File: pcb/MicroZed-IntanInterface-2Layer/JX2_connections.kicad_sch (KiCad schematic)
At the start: 25 parts, among them Q2 BSS138, U3 FT230XS

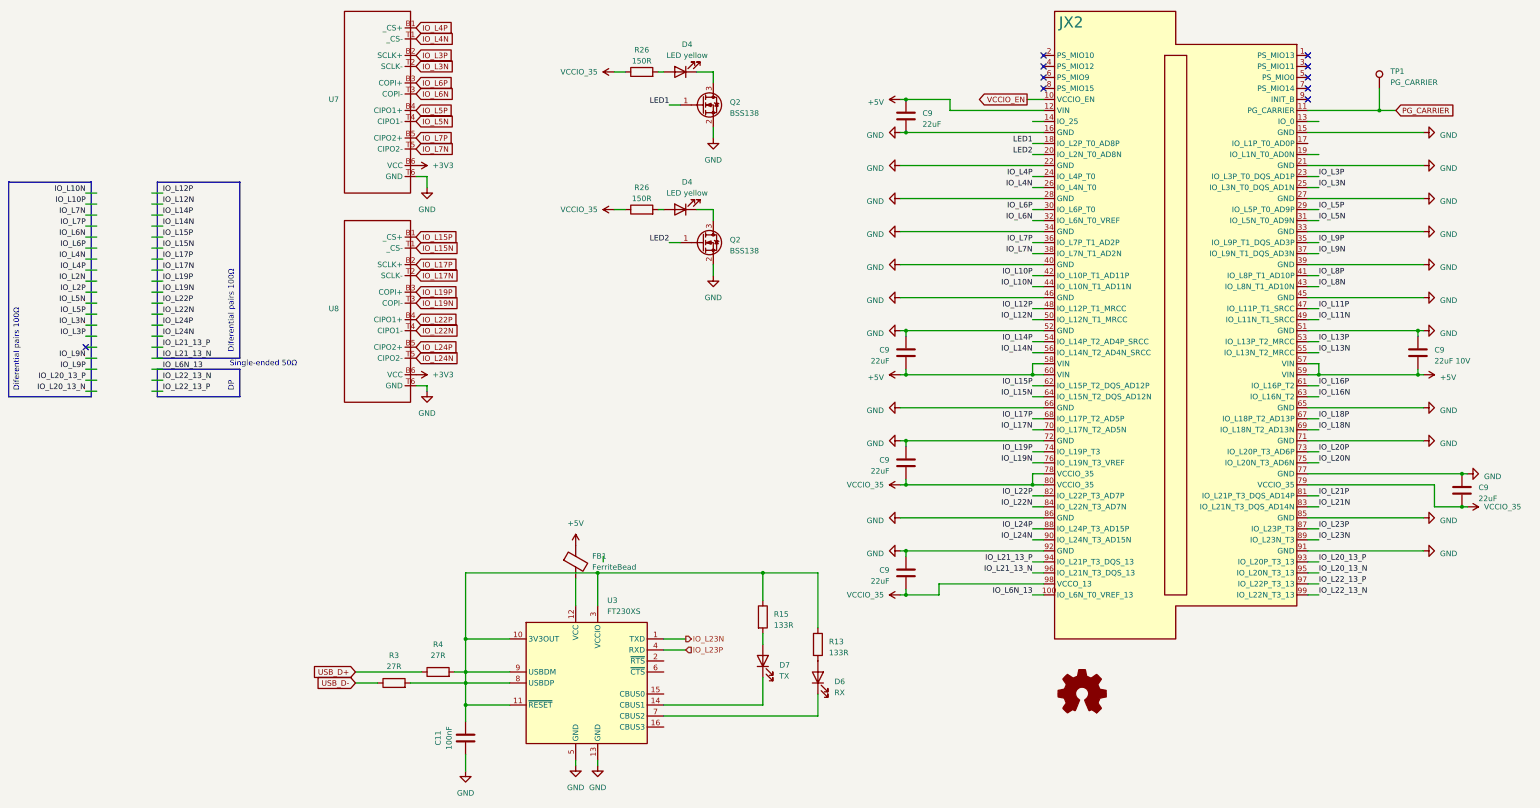
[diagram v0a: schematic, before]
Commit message: Updated PCB after v0.22 bug fixes
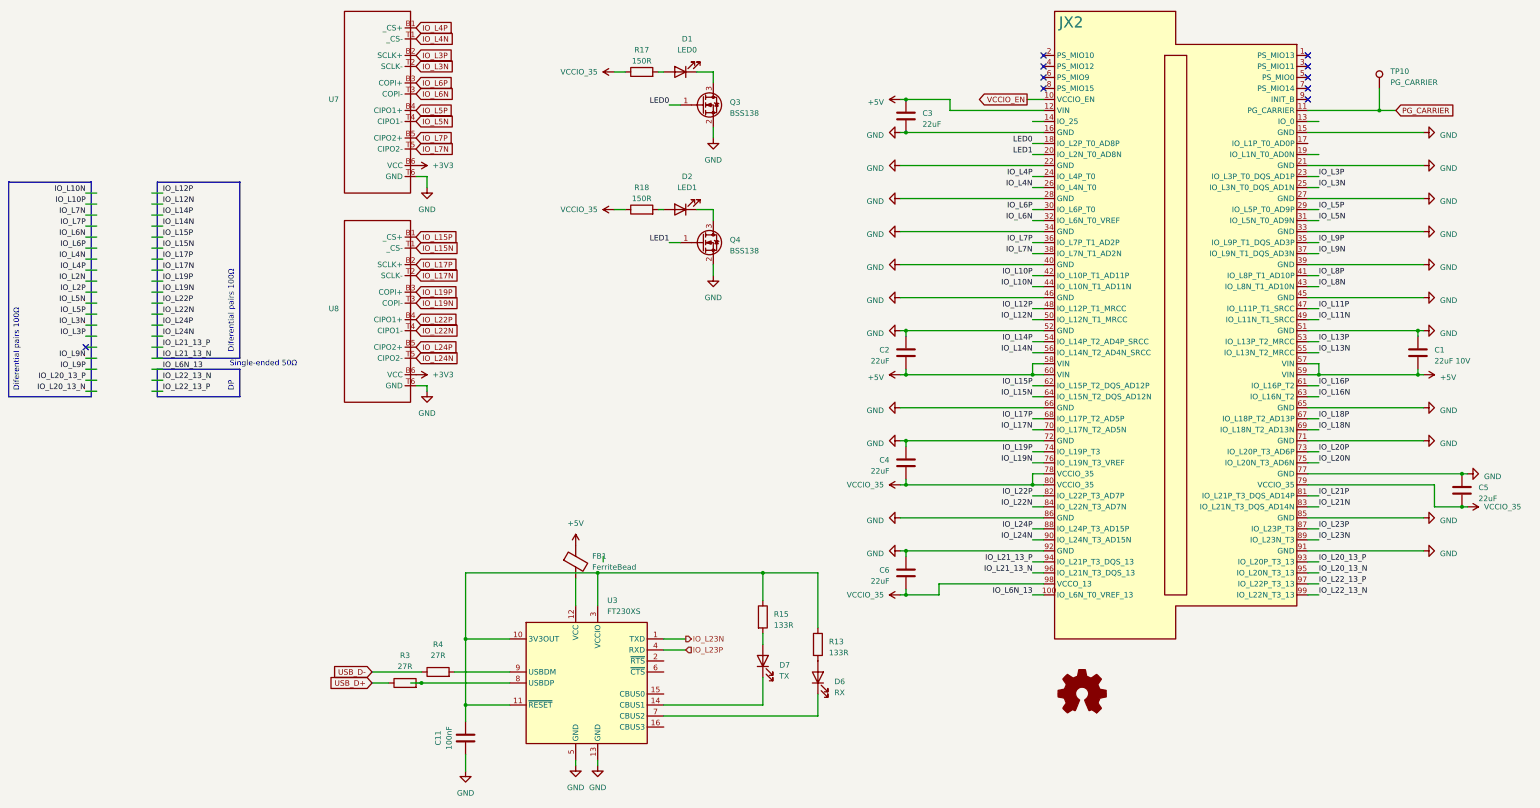
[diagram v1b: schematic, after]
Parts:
- removed D4 (x2): LED yellow, Viktor:LED0805, symbol Device:LED
- added D1: LED0, LED_SMD:LED_0603_1608Metric, symbol Device:LED
- added D2: LED1, LED_SMD:LED_0603_1608Metric, symbol Device:LED
- renumbered C9 to C1, C9 to C2, C9 to C3, C9 to C4, C9 to C5, C9 to C6, Q2 to Q3, Q2 to Q4, R26 to R17, R26 to R18, TP1 to TP10
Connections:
- net LED2 is gone; now on net LED1: JX2.20 (IO_L2N_T0_AD8N), Q4.1 (G)
- net LED1: no longer JX2.18 (IO_L2P_T0_AD8P), Q3.1 (G)
- net USB_D+: now also R3.1; no longer R4.1
- net USB_D-: now also R4.1; no longer R3.1
- net at C11.1, R13.1, R15.1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: no longer R3.2, R4.2, U3.8 (USBDP), U3.9 (USBDM)
- net at Q3.3 (D): now also D1.1 (K)
- net at Q4.3 (D): now also D2.1 (K)
- net at R17.2: now also D1.2 (A)
- net at R18.2: now also D2.2 (A)
- new net: R3.2, U3.8 (USBDP)
- new net: R4.2, U3.9 (USBDM)
- new net LED0: JX2.18 (IO_L2P_T0_AD8P), Q3.1 (G)
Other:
- moved on the sheet: R3

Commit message: Updates for version 1.0 to ship to UMich
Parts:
- C1: value 22uF 10V -> 22uF 25V; LCSC C5672 -> C12891
- C11: footprint Capacitor_SMD:C_0603_1608Metric -> Capacitor_SMD:C_0402_1005Metric; LCSC C66501 -> C307331
- C2, C3, C4, C5, C6: value 22uF -> 22uF 25V; LCSC C5672 -> C12891
- D1, D2, D6, D7: LCSC C2833058 -> C2286
- FB1: LCSC (none) -> C85840
- R13, R15: value 133R -> 150 1%; footprint Resistor_SMD:R_0603_1608Metric -> Resistor_SMD:R_0402_1005Metric; LCSC C4326496 -> C25082
- R17, R18: value 150R -> 150 1%; footprint Resistor_SMD:R_0603_1608Metric -> Resistor_SMD:R_0402_1005Metric; LCSC C22808 -> C25082
- R3, R4: value 27R -> 27; footprint Resistor_SMD:R_0603_1608Metric -> Resistor_SMD:R_0402_1005Metric; LCSC C4326496 -> C413051
- TP10: footprint Viktor:TestPoint__Drill1.0mm -> TestPoint:TestPoint_THTPad_D2.0mm_Drill1.0mm
- U3: LCSC (none) -> C69082
- U7, U8: now not fitted; now left out of the parts list
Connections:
- net VCCIO_35: now also D1.2 (A), D2.2 (A); no longer R17.1, R18.1
- net at Q3.3 (D): now also R17.2; no longer D1.1 (K)
- net at Q4.3 (D): now also R18.2; no longer D2.1 (K)
- new net: D1.1 (K), R17.1
- new net: D2.1 (K), R18.1
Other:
- moved on the sheet: D1, D2, R17, R18
